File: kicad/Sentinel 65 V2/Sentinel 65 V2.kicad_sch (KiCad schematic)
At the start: 159 parts, among them J1 SNES Controller, J10 SVGA Connector, J11 USB_C_Receptacle_PowerOnly_6P, J12 Conn_01x02, J13 Conn_01x02, J14 Internal Control Header (Opti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, J15 DV Header, J16 DEBUG SERIAL, J2 2x32 2.54mm Card Edge Connect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, J3 Clock Port, J4 SNES Controller, J5 SD_Card, J6 LEFT, J7 FPGA_PROG, J8 RIGHT, J9 Flash Enable, SW1 SW_Push, SW2 SW_Push, SW3 SW_Push, U1 ATF22LV10C, U10 LM1086IT-3.3, U11 MCP1316MT-33LE/OT, U2 W65C265S8PLG-8, U3 IS61WV5128EDBLL-10TLI, U4 SST39LF040-55-4C-NHE-T, U5 W25Q16JVSNIQ, U6 AP7361C-12E, U7 74CBTLV3126PW,118, U8 ICE40UP5K-SG48ITR, U9 WM8524CGEDT, X1 2MHz, X2 8Mhz, X3 25MHz

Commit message: Added PDF of schematic
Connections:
- net IRQ2: now also U1.22 (I/O); no longer U1.7 (IN)
- net IRQ3: now also U1.23 (I/O); no longer U1.8 (IN)
- net ~{IRQ}2: now also U1.7 (IN); no longer U1.22 (I/O)
- net ~{IRQ}3: now also U1.8 (IN); no longer U1.23 (I/O)
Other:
- moved on the sheet: J16, U2B, U2C

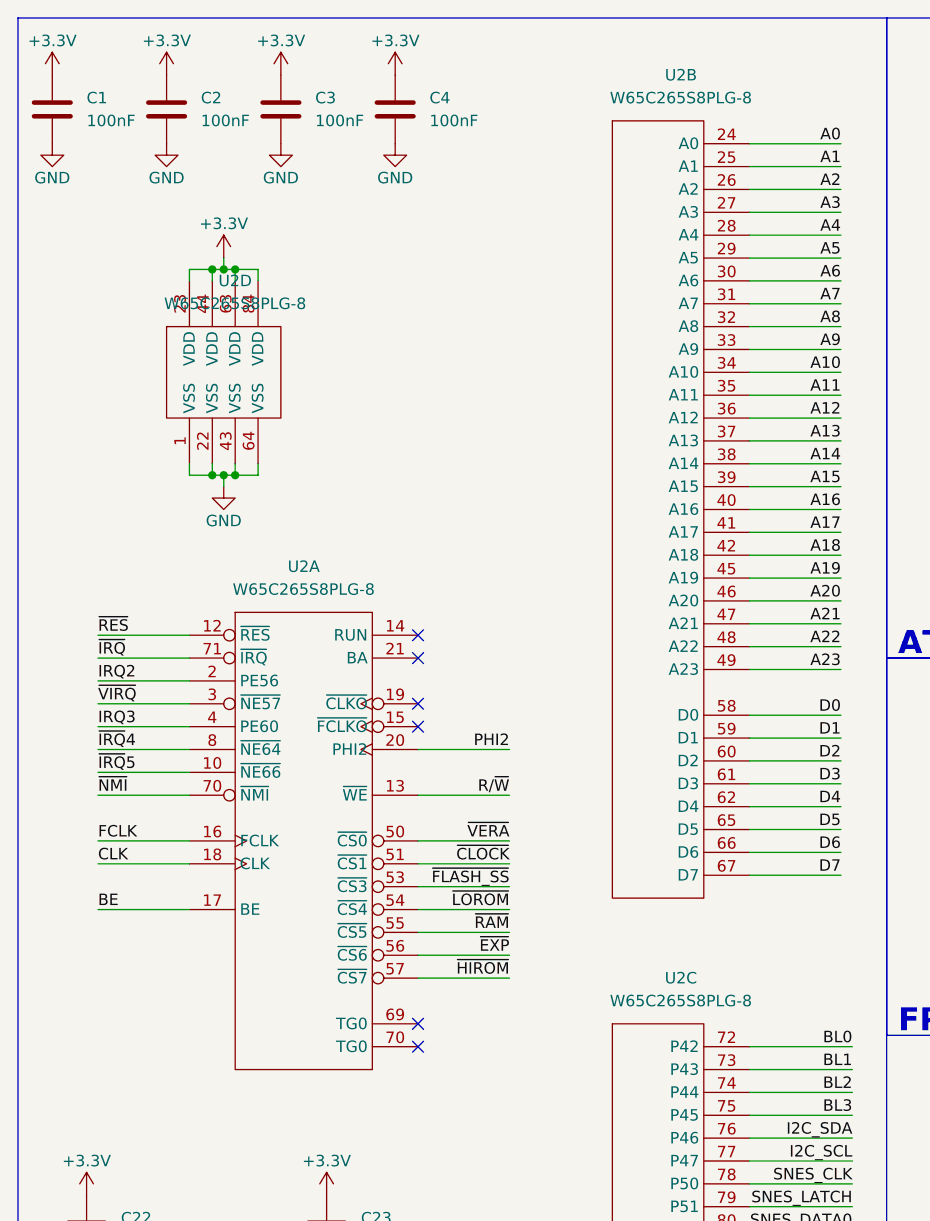
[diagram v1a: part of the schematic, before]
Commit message: Added PDF of schematic
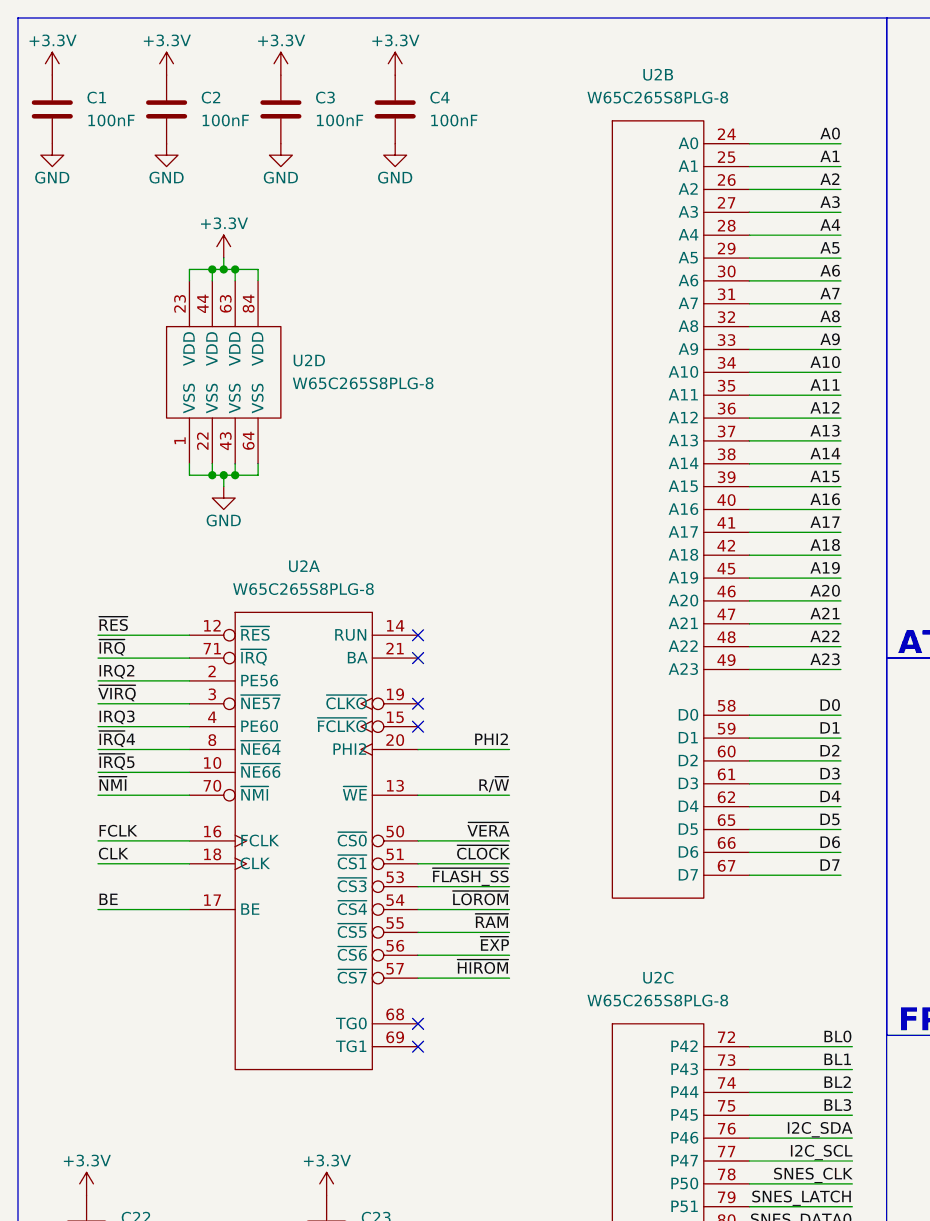
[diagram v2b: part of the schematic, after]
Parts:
- U2: footprint Package_LCC:PLCC-84_SMD-Socket -> Package_LCC:PLCC-84_THT-Socket

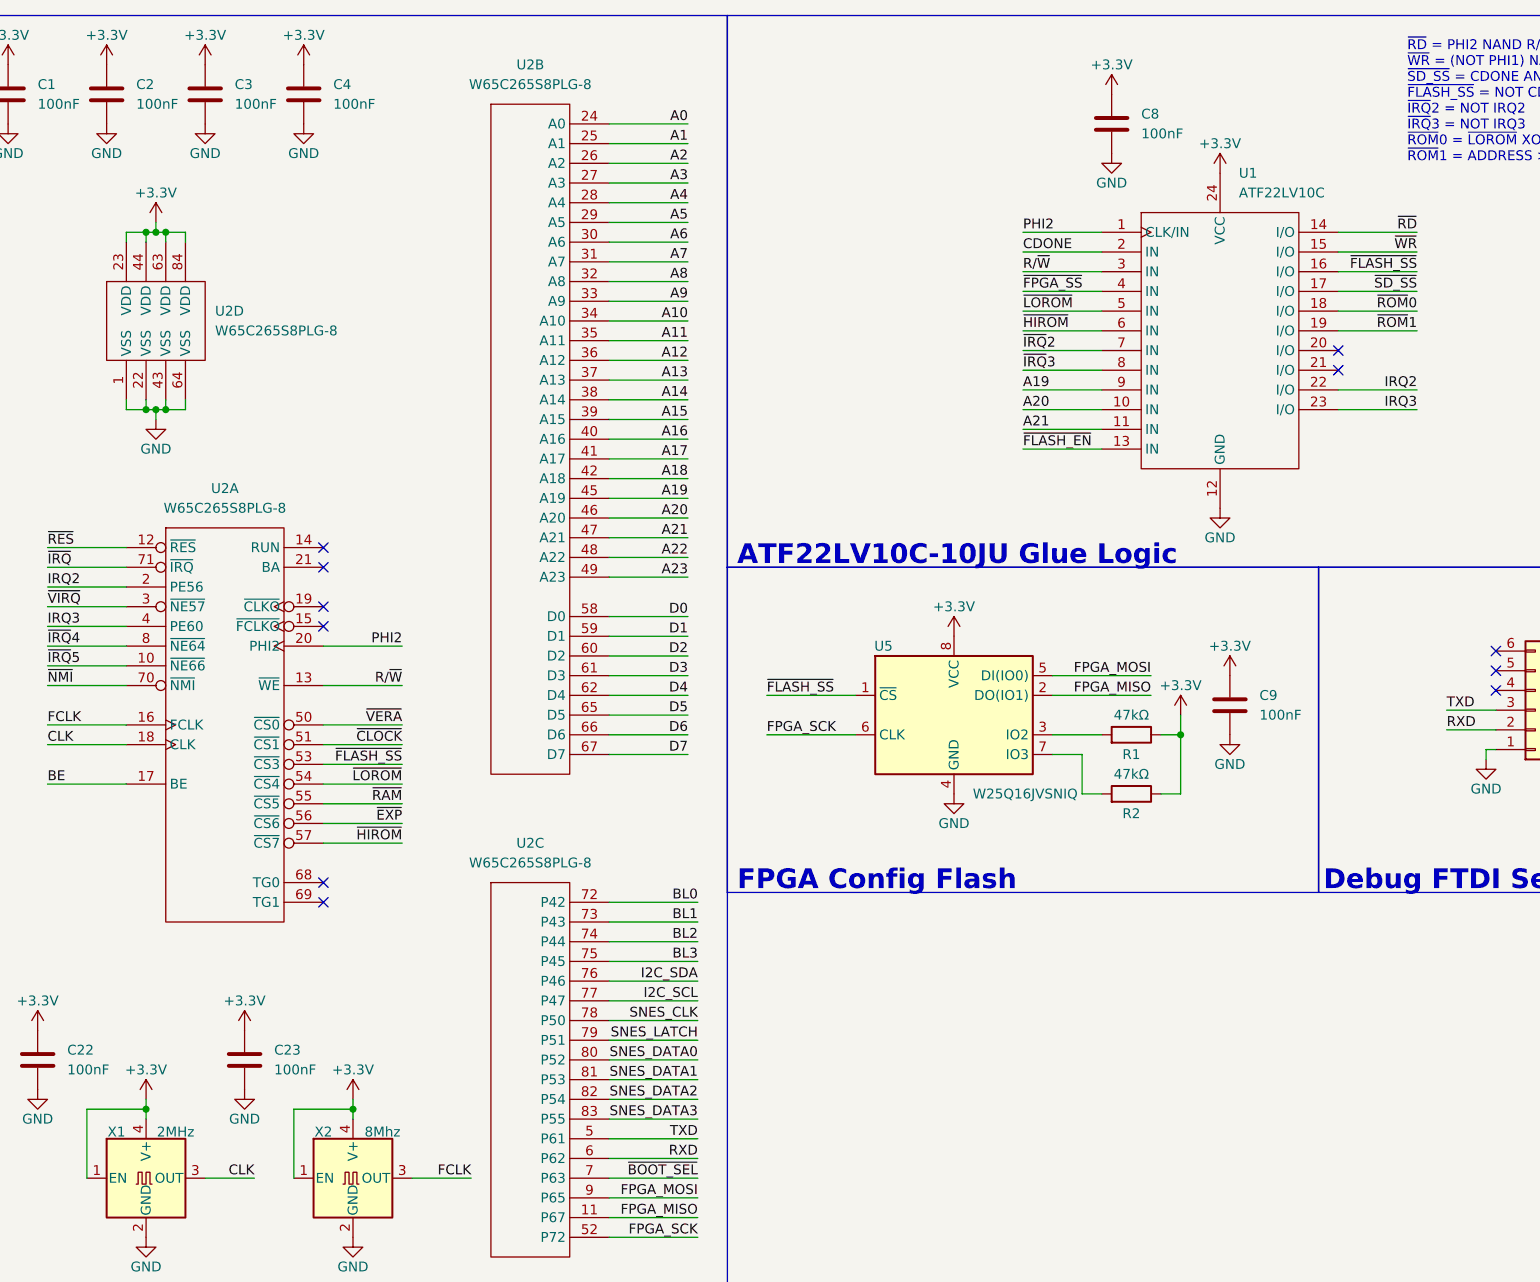
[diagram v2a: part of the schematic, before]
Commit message: Added datasheets and manuals
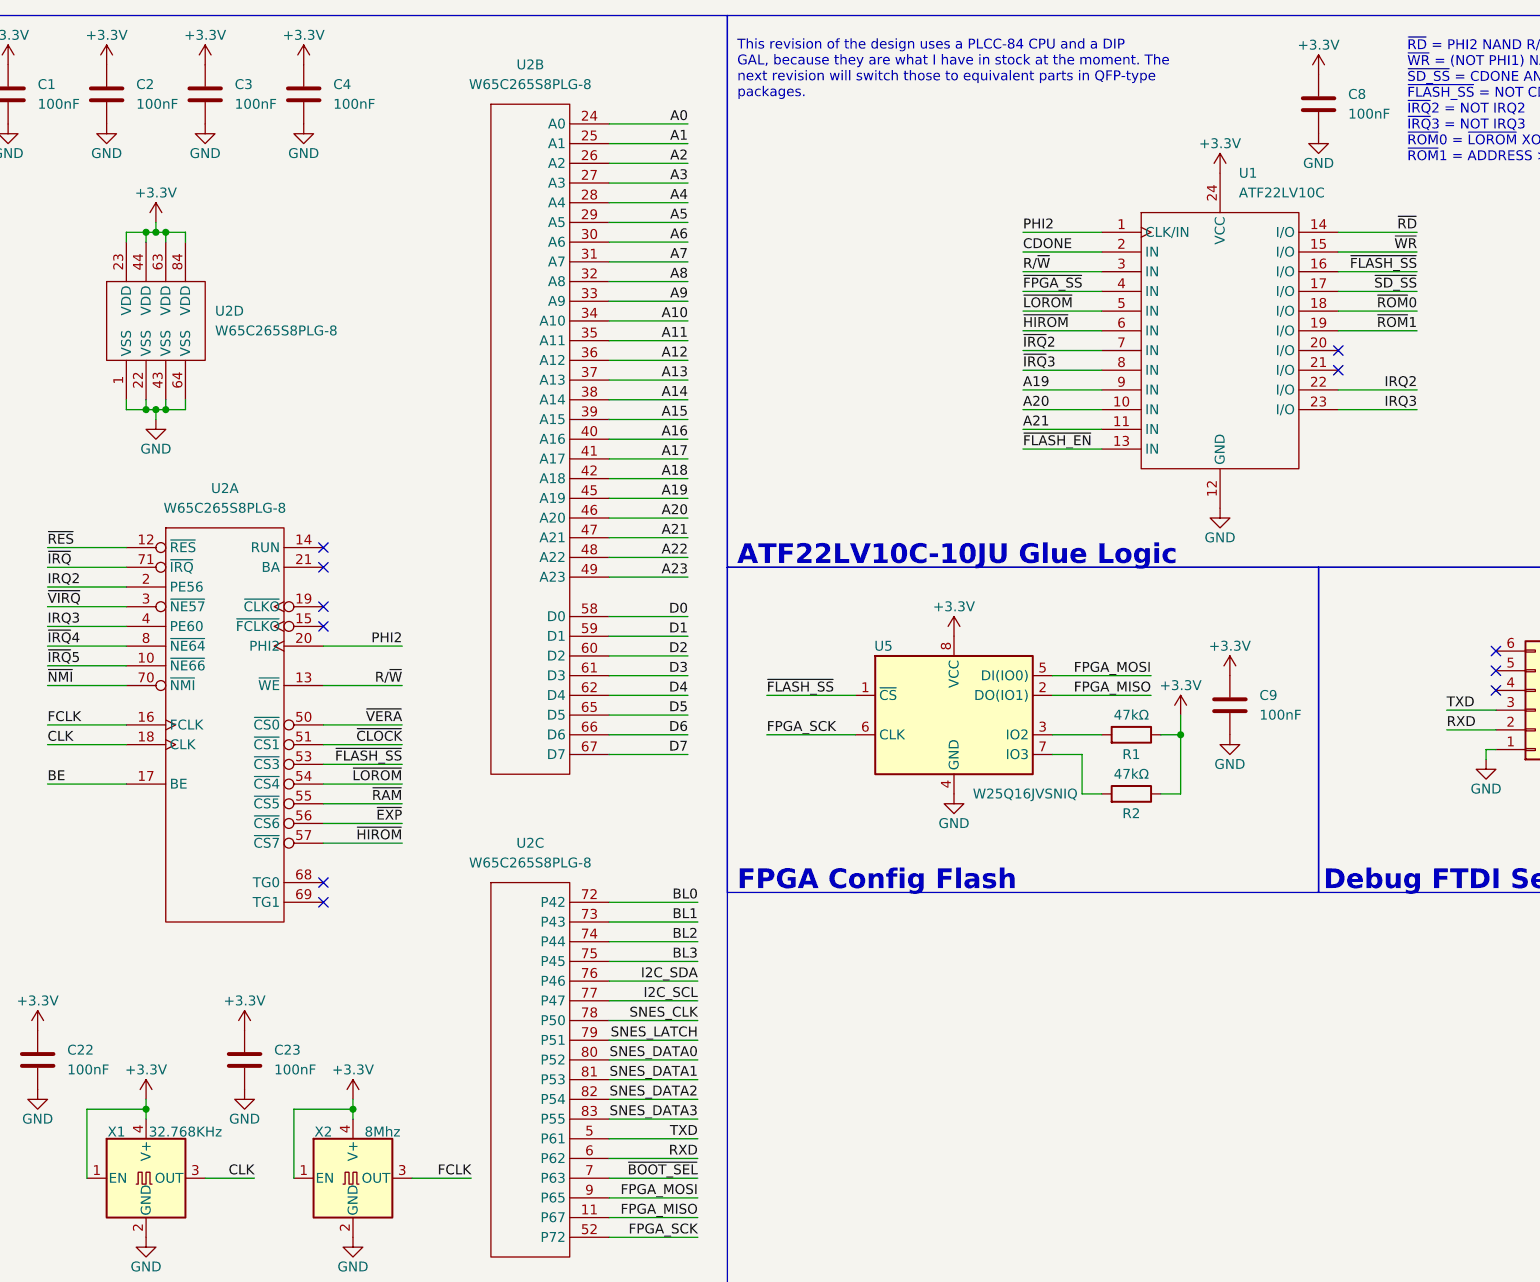
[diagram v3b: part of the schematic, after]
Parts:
- X1: value 2MHz -> 32.768KHz
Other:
- note added: "This revision of the design uses a PLCC-84 CPU and a DIP GAL, because they are what I have in stock at the moment. The next revision will switch those to equivalent parts in QFP-type packages."
- moved on the sheet: C8
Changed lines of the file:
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@@
     (effects (font (size 2.54 2.54) (thickness 0.508) bold) (justify left bottom))
   )
+  (text "This revision of the design uses a PLCC-84 CPU and a DIP\nGAL, because they are what I have in stock at the moment. The\nnext revision will switch those to equivalent parts in QFP-type\npackages."
+    (at 110.49 23.495 0)
+    (effects (font (size 1.27 1.27)) (justify left bottom))
+  )
   (label "~{RD}" (at 351.79 54.61 0) (fields_autoplaced)
     (effects (font (size 1.27 1.27)) (justify left bottom))
@@
     )
   )
-  (symbol (lib_id "power:+3.3V") (at 158.75 22.86 0) (unit 1)
+  (symbol (lib_id "power:+3.3V") (at 185.42 20.32 0) (unit 1)
     (in_bom yes) (on_board yes) (dnp no)
-    (property "Reference" "#PWR08" (at 158.75 26.67 0)
+    (property "Reference" "#PWR08" (at 185.42 24.13 0)
       (effects (font (size 1.27 1.27)) hide)
     )
-    (property "Value" "+3.3V" (at 158.75 19.05 0)
+    (property "Value" "+3.3V" (at 185.42 16.51 0)
       (effects (font (size 1.27 1.27)))
     )
-    (property "Footprint" "" (at 158.75 22.86 0)
+    (property "Footprint" "" (at 185.42 20.32 0)
       (effects (font (size 1.27 1.27)) hide)
     )
-    (property "Datasheet" "" (at 158.75 22.86 0)
+    (property "Datasheet" "" (at 185.42 20.32 0)
       (effects (font (size 1.27 1.27)) hide)
     )
@@
     )
   )
-  (symbol (lib_id "Device:C") (at 158.75 26.67 0) (unit 1)
+  (symbol (lib_id "Device:C") (at 185.42 24.13 0) (unit 1)
     (in_bom yes) (on_board yes) (dnp no) (fields_autoplaced)
-    (property "Reference" "C8" (at 162.56 25.3999 0)
+    (property "Reference" "C8" (at 189.23 22.8599 0)
       (effects (font (size 1.27 1.27)) (justify left))
     )
-    (property "Value" "100nF" (at 162.56 27.9399 0)
+    (property "Value" "100nF" (at 189.23 25.3999 0)
       (effects (font (size 1.27 1.27)) (justify left))
     )
-    (property "Footprint" "Capacitor_SMD:C_0402_1005Metric" (at 159.7152 30.48 0)
+    (property "Footprint" "Capacitor_SMD:C_0402_1005Metric" (at 186.3852 27.94 0)
       (effects (font (size 1.27 1.27)) hide)
     )
-    (property "Datasheet" "~" (at 158.75 26.67 0)
+    (property "Datasheet" "~" (at 185.42 24.13 0)
       (effects (font (size 1.27 1.27)) hide)
     )
@@
       (effects (font (size 1.27 1.27)))
     )
-    (property "Value" "2MHz" (at 38.1 156.6005 0)
+    (property "Value" "32.768KHz" (at 39.37 156.6005 0)
       (effects (font (size 1.27 1.27)))
     )
@@
     )
   )
-  (symbol (lib_id "power:GND") (at 158.75 30.48 0) (unit 1)
+  (symbol (lib_id "power:GND") (at 185.42 27.94 0) (unit 1)
     (in_bom yes) (on_board yes) (dnp no)
-    (property "Reference" "#PWR018" (at 158.75 36.83 0)
+    (property "Reference" "#PWR018" (at 185.42 34.29 0)
       (effects (font (size 1.27 1.27)) hide)
     )
-    (property "Value" "GND" (at 158.75 34.29 0)
+    (property "Value" "GND" (at 185.42 31.75 0)
       (effects (font (size 1.27 1.27)))
     )
-    (property "Footprint" "" (at 158.75 30.48 0)
+    (property "Footprint" "" (at 185.42 27.94 0)
       (effects (font (size 1.27 1.27)) hide)
     )
-    (property "Datasheet" "" (at 158.75 30.48 0)
+    (property "Datasheet" "" (at 185.42 27.94 0)
       (effects (font (size 1.27 1.27)) hide)
     )

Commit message: Pinouts updated
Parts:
- removed J15: DV Header, symbol Connector_Generic:Conn_02x10_Odd_Even
- removed J16: DEBUG SERIAL, symbol Connector_Generic:Conn_01x06
- removed J3: Clock Port, symbol Connector_Generic:Conn_02x11_Odd_Even
- added J15: Conn_02x11_Odd_Even, symbol Connector_Generic:Conn_02x11_Odd_Even
- added J3: Conn_02x12_Odd_Even, symbol Connector_Generic:Conn_02x12_Odd_Even
- added JP1: Jumper_3_Open, Jumper:SolderJumper-3_P2.0mm_Open_TrianglePad1.0x1.5mm_NumberLabels, symbol Jumper:Jumper_3_Open
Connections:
- net +3.3V: now also J15.22 (Pin_22), J3.2 (Pin_2)
- net A0: now also J2.b3 (Pin_b3), J3.16 (Pin_16); no longer J2.a3 (Pin_a3)
- net A1: now also J2.a3 (Pin_a3), J3.15 (Pin_15); no longer J2.a4 (Pin_a4)
- net A10: now also J2.b8 (Pin_b8); no longer J2.a13 (Pin_a13)
- net A11: now also J2.a8 (Pin_a8); no longer J2.a14 (Pin_a14)
- net A12: now also J2.b9 (Pin_b9); no longer J2.a15 (Pin_a15)
- net A13: now also J2.a9 (Pin_a9); no longer J2.a16 (Pin_a16)
- net A14: now also J2.b10 (Pin_b10); no longer J2.a17 (Pin_a17)
- net A15: now also J2.a10 (Pin_a10); no longer J2.b11 (Pin_b11)
- net A16: now also J2.b11 (Pin_b11); no longer J2.b10 (Pin_b10)
- net A17: now also J2.a11 (Pin_a11); no longer J2.b9 (Pin_b9)
- net A18: now also J2.b12 (Pin_b12); no longer J2.b8 (Pin_b8)
- net A19: now also J2.a12 (Pin_a12); no longer J2.b7 (Pin_b7)
- net A2: now also J2.b4 (Pin_b4), J3.14 (Pin_14); no longer J2.a5 (Pin_a5)
- net A20: now also J2.b13 (Pin_b13); no longer J2.b6 (Pin_b6)
- net A21: now also J2.a13 (Pin_a13); no longer J2.b5 (Pin_b5)
- net A22: now also J2.b14 (Pin_b14); no longer J2.b4 (Pin_b4)
- net A23: now also J2.a14 (Pin_a14); no longer J2.b3 (Pin_b3)
- net A3: now also J2.a4 (Pin_a4), J3.13 (Pin_13); no longer J2.a6 (Pin_a6)
- net A4: now also J2.b5 (Pin_b5); no longer J2.a7 (Pin_a7)
- net A5: now also J2.a5 (Pin_a5); no longer J2.a8 (Pin_a8)
- net A6: now also J2.b6 (Pin_b6); no longer J2.a9 (Pin_a9)
- net A7: now also J2.a6 (Pin_a6); no longer J2.a10 (Pin_a10)
- net A8: now also J2.b7 (Pin_b7); no longer J2.a11 (Pin_a11)
- net A9: now also J2.a7 (Pin_a7); no longer J2.a12 (Pin_a12)
- net ADATA: now also J15.3 (Pin_3)
- net B0: now also J15.13 (Pin_13)
- net B1: now also J15.14 (Pin_14)
- net B2: now also J15.15 (Pin_15)
- net B3: now also J15.16 (Pin_16)
- net BCK: now also J15.1 (Pin_1)
- net CLK: now also U11.1 (~{RES})
- net D0: now also J2.b20 (Pin_b20), J3.24 (Pin_24); no longer J2.a20 (Pin_a20)
- net D1: now also J2.a20 (Pin_a20), J3.23 (Pin_23); no longer J2.a21 (Pin_a21)
- net D2: now also J2.b21 (Pin_b21), J3.22 (Pin_22); no longer J2.a22 (Pin_a22)
- net D3: now also J2.a21 (Pin_a21), J3.21 (Pin_21); no longer J2.a23 (Pin_a23)
- net D4: now also J2.b22 (Pin_b22), J3.20 (Pin_20); no longer J2.a24 (Pin_a24)
- net D5: now also J2.a22 (Pin_a22), J3.19 (Pin_19); no longer J2.a25 (Pin_a25)
- net D6: now also J2.b23 (Pin_b23), J3.18 (Pin_18); no longer J2.a26 (Pin_a26)
- net D7: now also J2.a23 (Pin_a23), J3.17 (Pin_17); no longer J2.a27 (Pin_a27)
- net G0: now also J15.9 (Pin_9)
- net G1: now also J15.10 (Pin_10)
- net G2: now also J15.11 (Pin_11)
- net G3: now also J15.12 (Pin_12)
- net GND: now also J15.20 (Pin_20), J15.21 (Pin_21), J3.1 (Pin_1)
- net HSYNC: now also J15.17 (Pin_17)
- net I2C_SCL: now also J2.a27 (Pin_a27), J3.4 (Pin_4); no longer J2.b22 (Pin_b22)
- net I2C_SDA: now also J2.a28 (Pin_a28), J3.6 (Pin_6); no longer J2.b23 (Pin_b23)
- net LRCK: now also J15.2 (Pin_2)
- net PHI2: now also J3.9 (Pin_9), JP1.2 (C); no longer U8.36 (IOT_48b)
- net R0: now also J15.5 (Pin_5)
- net R1: now also J15.6 (Pin_6)
- net R2: now also J15.7 (Pin_7)
- net R3: now also J15.8 (Pin_8)
- net RXD: now also J3.5 (Pin_5)
- net SNES_CLK: now also J2.a30 (Pin_a30); no longer J2.a29 (Pin_a29)
- net SNES_DATA0: now also J2.b27 (Pin_b27); no longer J2.b24 (Pin_b24)
- net SNES_DATA1: now also J2.b28 (Pin_b28); no longer J2.b25 (Pin_b25)
- net SNES_DATA2: now also J2.b29 (Pin_b29); no longer J2.b19 (Pin_b19)
- net SNES_DATA3: now also J2.b30 (Pin_b30); no longer J2.b15 (Pin_b15)
- net SNES_LATCH: now also J2.a29 (Pin_a29); no longer J2.a28 (Pin_a28)
- net SYSCLK: now also J15.4 (Pin_4)
- net TXD: now also J3.3 (Pin_3)
- net VSYNC: now also J15.18 (Pin_18)
- net ~{BOOT_SEL}: no longer U11.1 (~{RES})
- net ~{CLOCK}: now also J3.10 (Pin_10)
- net ~{IRQ}: now also J2.a24 (Pin_a24); no longer J2.b20 (Pin_b20)
- net ~{IRQ}2: now also J3.8 (Pin_8)
- net ~{IRQ}3: now also J2.b24 (Pin_b24); no longer J2.b26 (Pin_b26)
- net ~{IRQ}4: now also J2.b25 (Pin_b25); no longer J2.b13 (Pin_b13)
- net ~{IRQ}5: now also J2.a25 (Pin_a25); no longer J2.b14 (Pin_b14)
- net ~{NMI}: now also J2.b26 (Pin_b26); no longer J2.b21 (Pin_b21)
- net ~{RAM}: now also J2.b19 (Pin_b19); no longer J2.b27 (Pin_b27)
- net ~{RD}: now also J2.a16 (Pin_a16), J3.11 (Pin_11); no longer J2.b12 (Pin_b12)
- net ~{RES}: now also J3.7 (Pin_7)
- net ~{WR}: now also J3.12 (Pin_12)
- new net PXCLK: J15.19 (Pin_19), JP1.3 (B)
- new net VCLK: JP1.1 (A), U8.36 (IOT_48b)
- no-connect marks 25 -> 22
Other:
- note added: "Clock/Debug Port"
- note added: "VERA Clock"
- note removed: "Clock Port"
- note removed: "Debug FTDI Serial Port"
- note removed: "Once the system has booted, ~{BOOT_SEL} switches to output mode, and acts to feed the watchdog input via a timer interrupt."
- moved on the sheet: U8C
